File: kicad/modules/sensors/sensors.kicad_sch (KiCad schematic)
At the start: 68 parts, among them J1 Bus_PCI_Express_x1, J2 TYPE-C-31-M-04, J3 Conn_01x02, U2 RP2040, U3 TPS2121RUXR, U4 W25Q128JVP, U5 BMP388, U6 LMR51430 1.1k FPWM, U7 TPS63070RNMR, U8 BNO055, U9 MCP25625T-E/ML, X1 ABM8-272-T3, Y1 ABS07-32.768KHZ-T, Y2 X322516MLB4SI

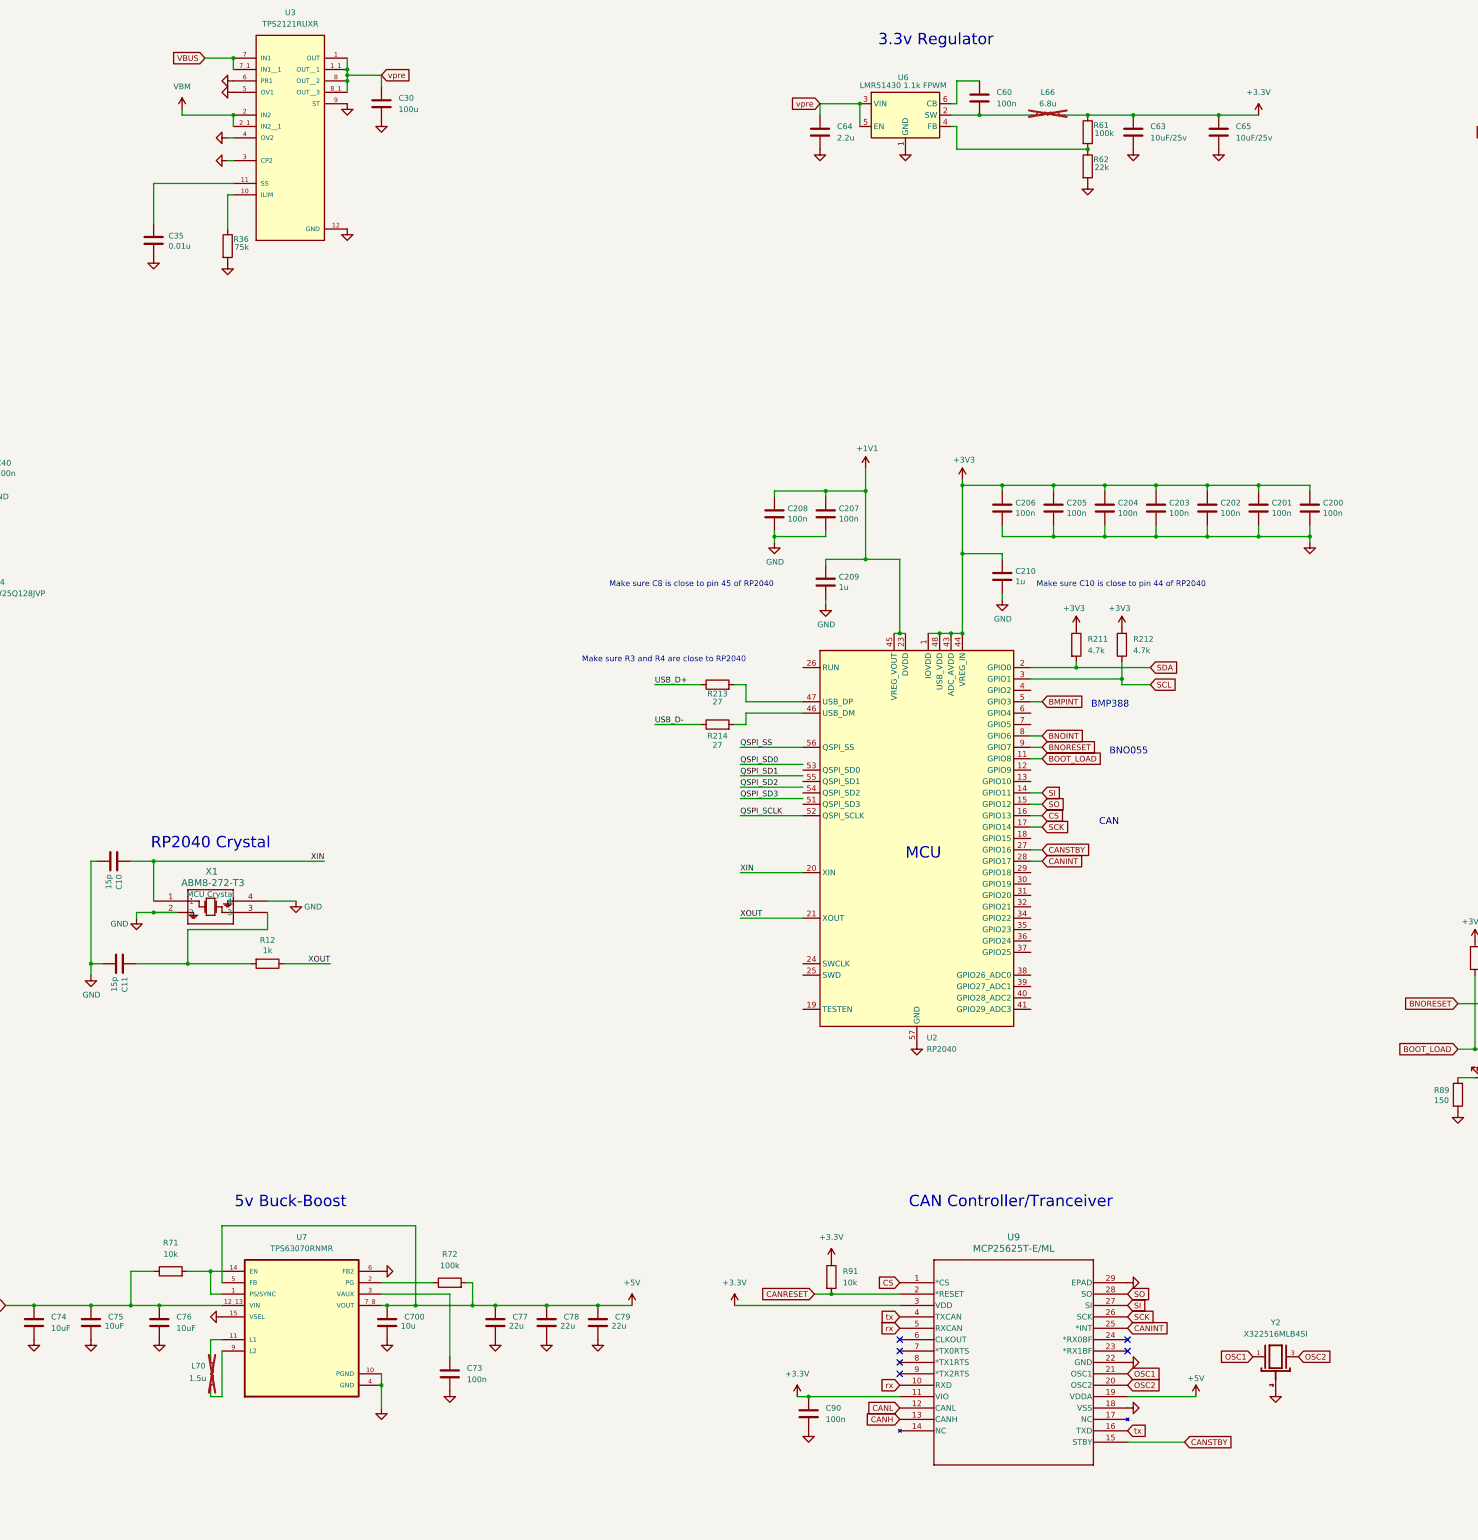
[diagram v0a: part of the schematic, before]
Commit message: update symbol library to use project specific library
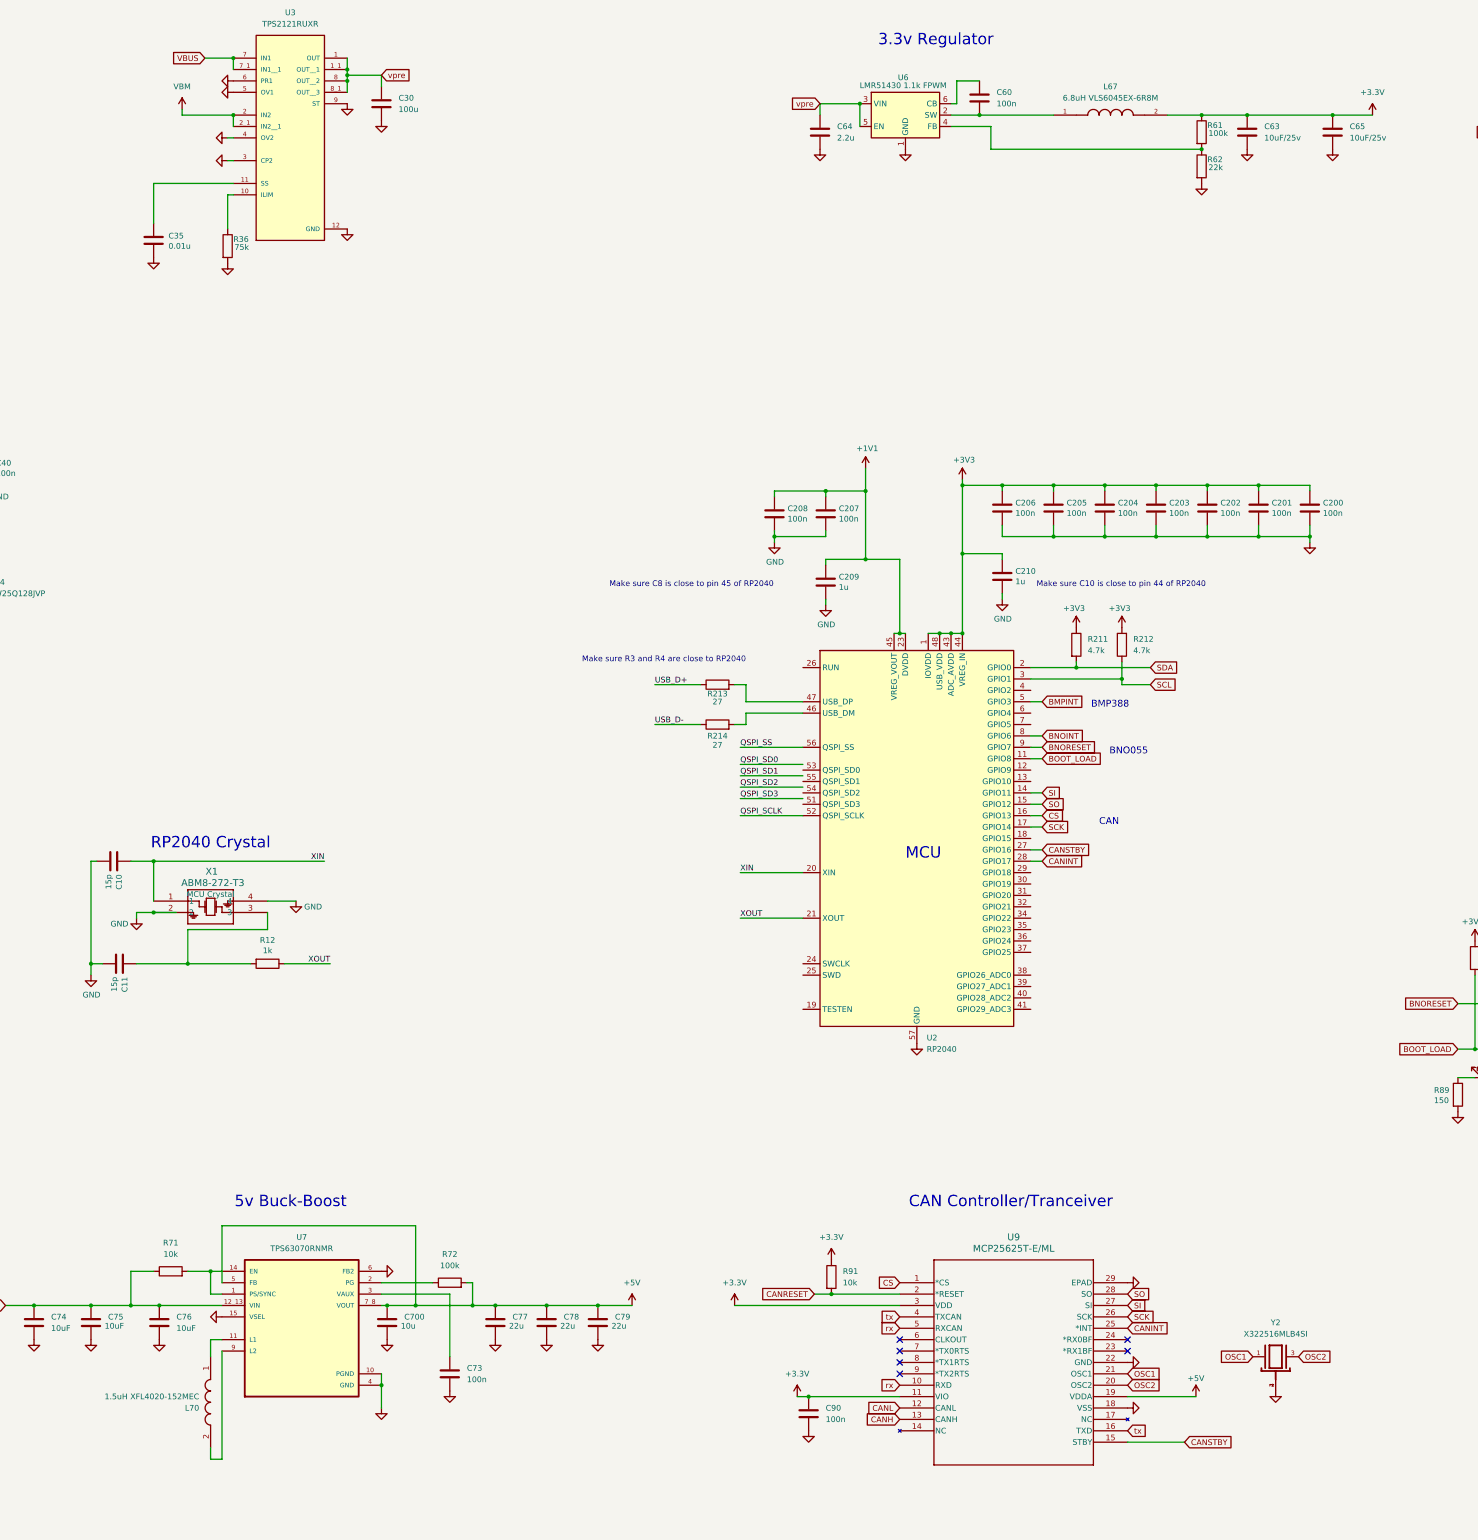
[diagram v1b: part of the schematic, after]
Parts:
- removed L66: 6.8u, symbol Device:L
- removed L70: 1.5u, symbol Device:L
- added L67: 6.8uH VLS6045EX-6R8M, VLS6045EX-6R8M:IND_VLS6045EX-6R8M, symbol VLS6045EX-6R8M:VLS6045EX-6R8M
- added L70: 1.5uH XFL4020-152MEC, 1.5uH:XFL4020152MEC, symbol XFL4020-152MEC:XFL4020-152MEC
- U9: footprint MCP25625:QFN28_6X6MC_MCH -> MCP25625T_E_ML:QFN28_6X6MC_MCH
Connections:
- net +3.3V: now also L67.2
- net at C60.2, U6.2 (SW): now also L67.1
- net at U7.11 (L1): now also L70.1
- net at U7.9 (L2): now also L70.2
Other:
- moved on the sheet: C63, C65, R61, R62

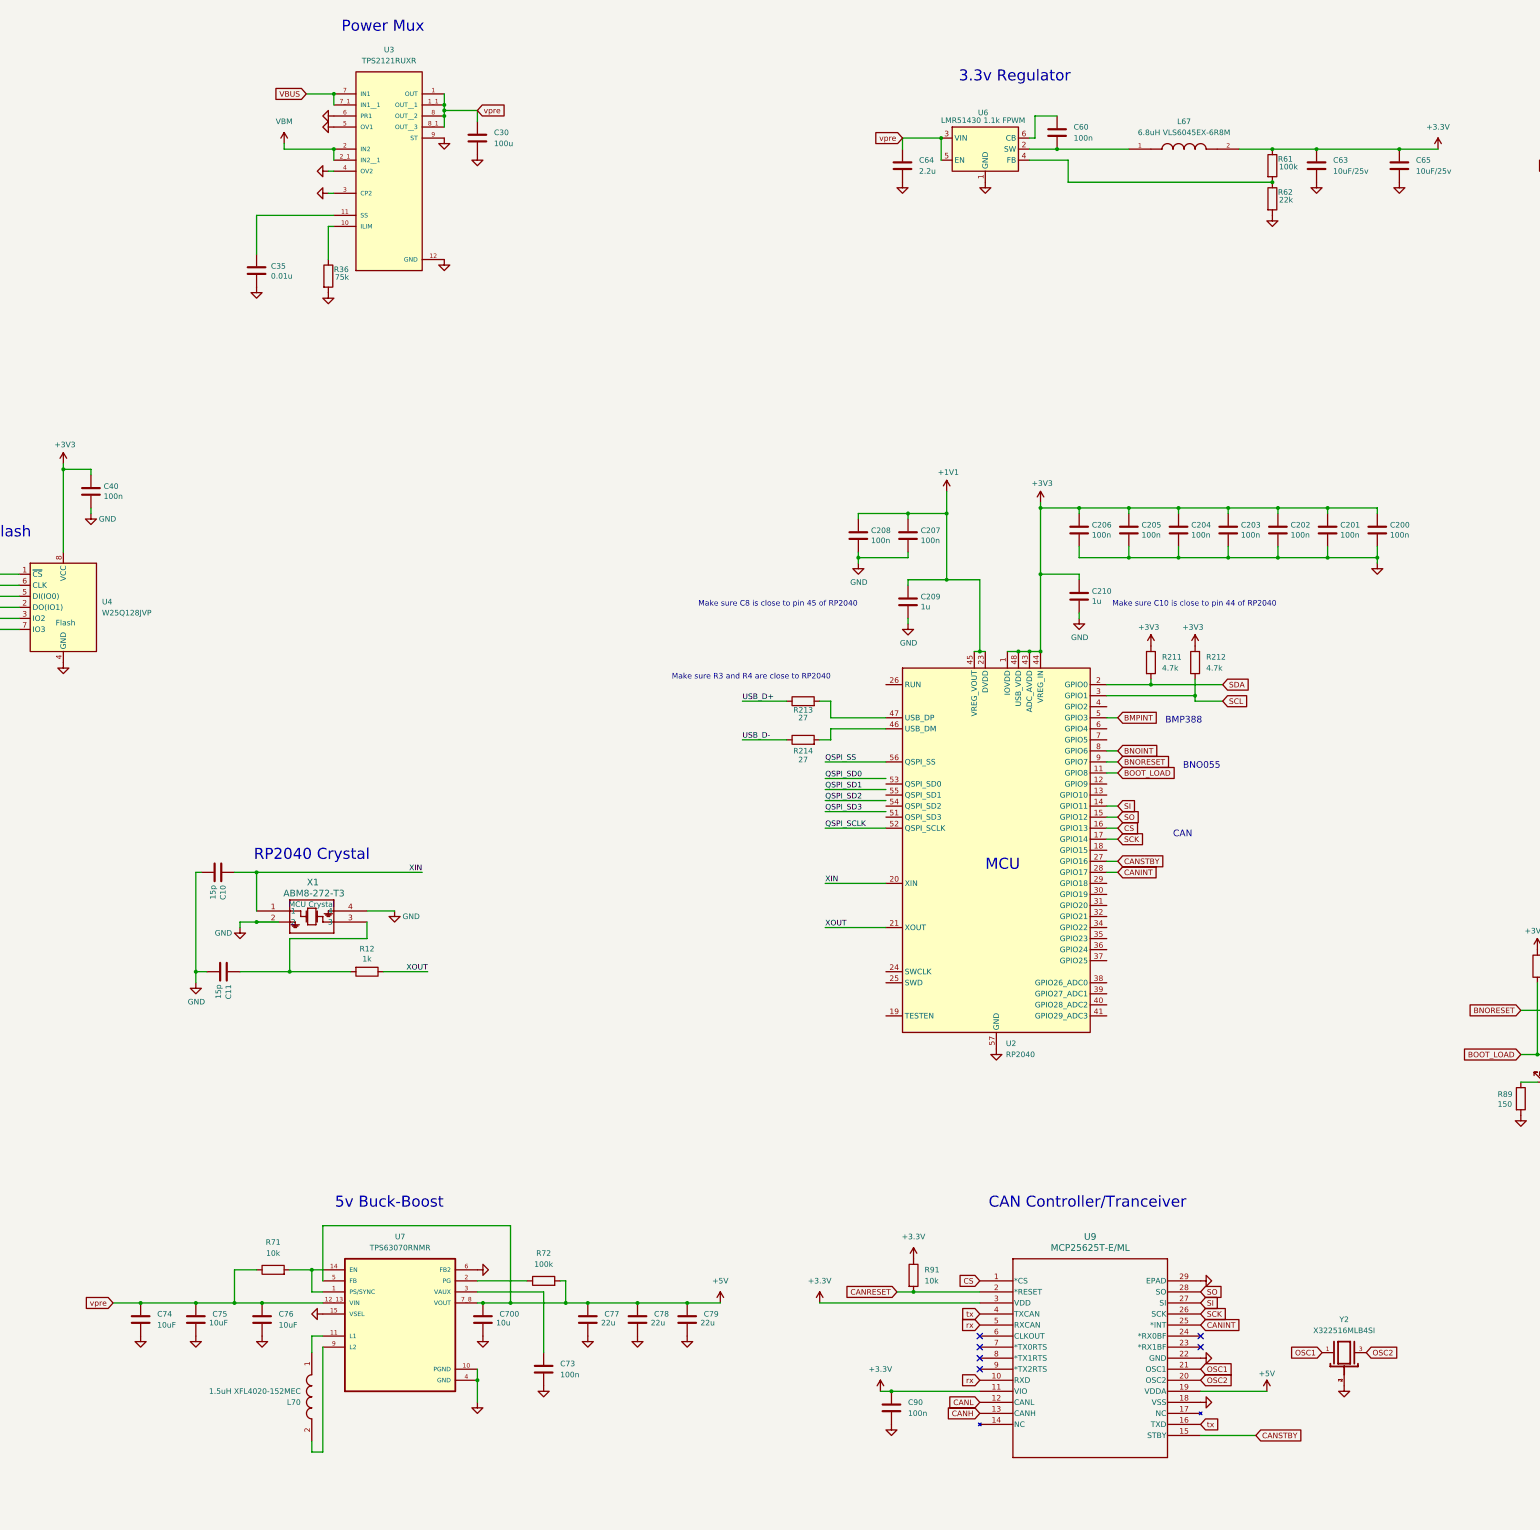
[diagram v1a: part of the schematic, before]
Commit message: delete regs and mux
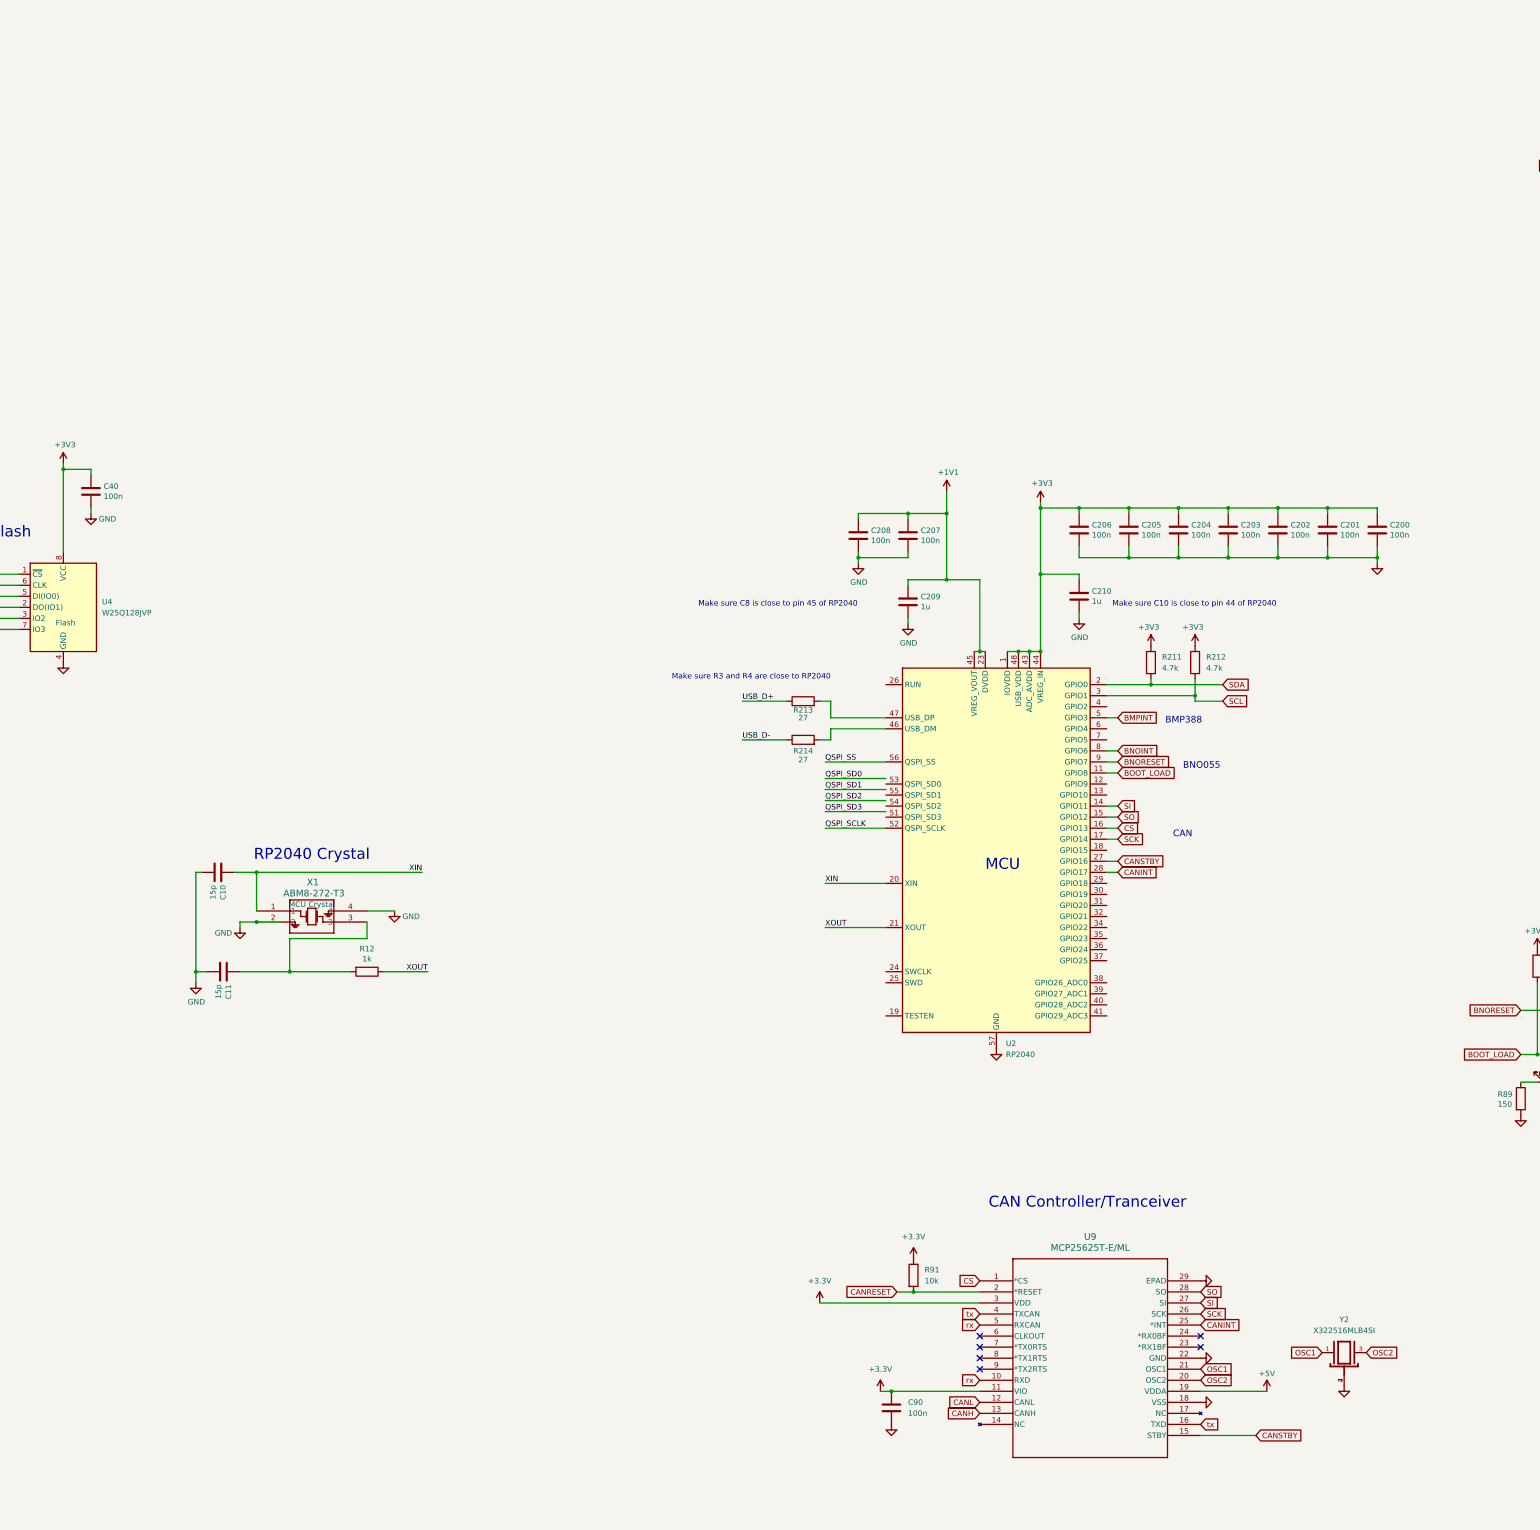
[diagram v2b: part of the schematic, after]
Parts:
- removed C30: 100u, Capacitor_SMD:C_1206_3216Metric, symbol Device:C
- removed C35: 0.01u, Capacitor_SMD:C_0402_1005Metric, symbol Device:C
- removed C60, C73: 100n, Capacitor_SMD:C_0402_1005Metric, symbol Device:C
- removed C63, C65: 10uF/25v, Capacitor_SMD:C_0603_1608Metric, symbol Device:C
- removed C64: 2.2u, Capacitor_SMD:C_0402_1005Metric, symbol Device:C
- removed C700: 10u, Capacitor_SMD:C_0402_1005Metric, symbol Device:C
- removed C74, C75, C76: 10uF, Capacitor_SMD:C_0402_1005Metric, symbol Device:C
- removed C77, C78, C79: 22u, Capacitor_SMD:C_0402_1005Metric, symbol Device:C
- removed L67: 6.8uH VLS6045EX-6R8M, VLS6045EX-6R8M:IND_VLS6045EX-6R8M, symbol VLS6045EX-6R8M:VLS6045EX-6R8M
- removed L70: 1.5uH XFL4020-152MEC, 1.5uH:XFL4020152MEC, symbol XFL4020-152MEC:XFL4020-152MEC
- removed R36: 75k, Resistor_SMD:R_0603_1608Metric, symbol Device:R
- removed R61, R72: 100k, Resistor_SMD:R_0402_1005Metric, symbol Device:R
- removed R62: 22k, Resistor_SMD:R_0402_1005Metric, symbol Device:R
- removed R71: 10k, Resistor_SMD:R_0402_1005Metric, symbol Device:R
- removed U3: TPS2121RUXR, TPS2121RUXR:IC_TPS2121RUXR, symbol TPS2121RUXR:TPS2121RUXR
- removed U6: LMR51430 1.1k FPWM, Package_TO_SOT_SMD:SOT-23-6, symbol Regulator_Switching:LMR51430
- removed U7: TPS63070RNMR, TPS63070RNMR:VREG_TPS63070RNMR, symbol TPS63070RNMR:TPS63070RNMR
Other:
- note removed: "3.3v Regulator"
- note removed: "5v Buck-Boost"
- note removed: "Power Mux"
